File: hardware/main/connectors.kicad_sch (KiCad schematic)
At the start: 3 parts, among them J501 J_UI, J502 J_LED

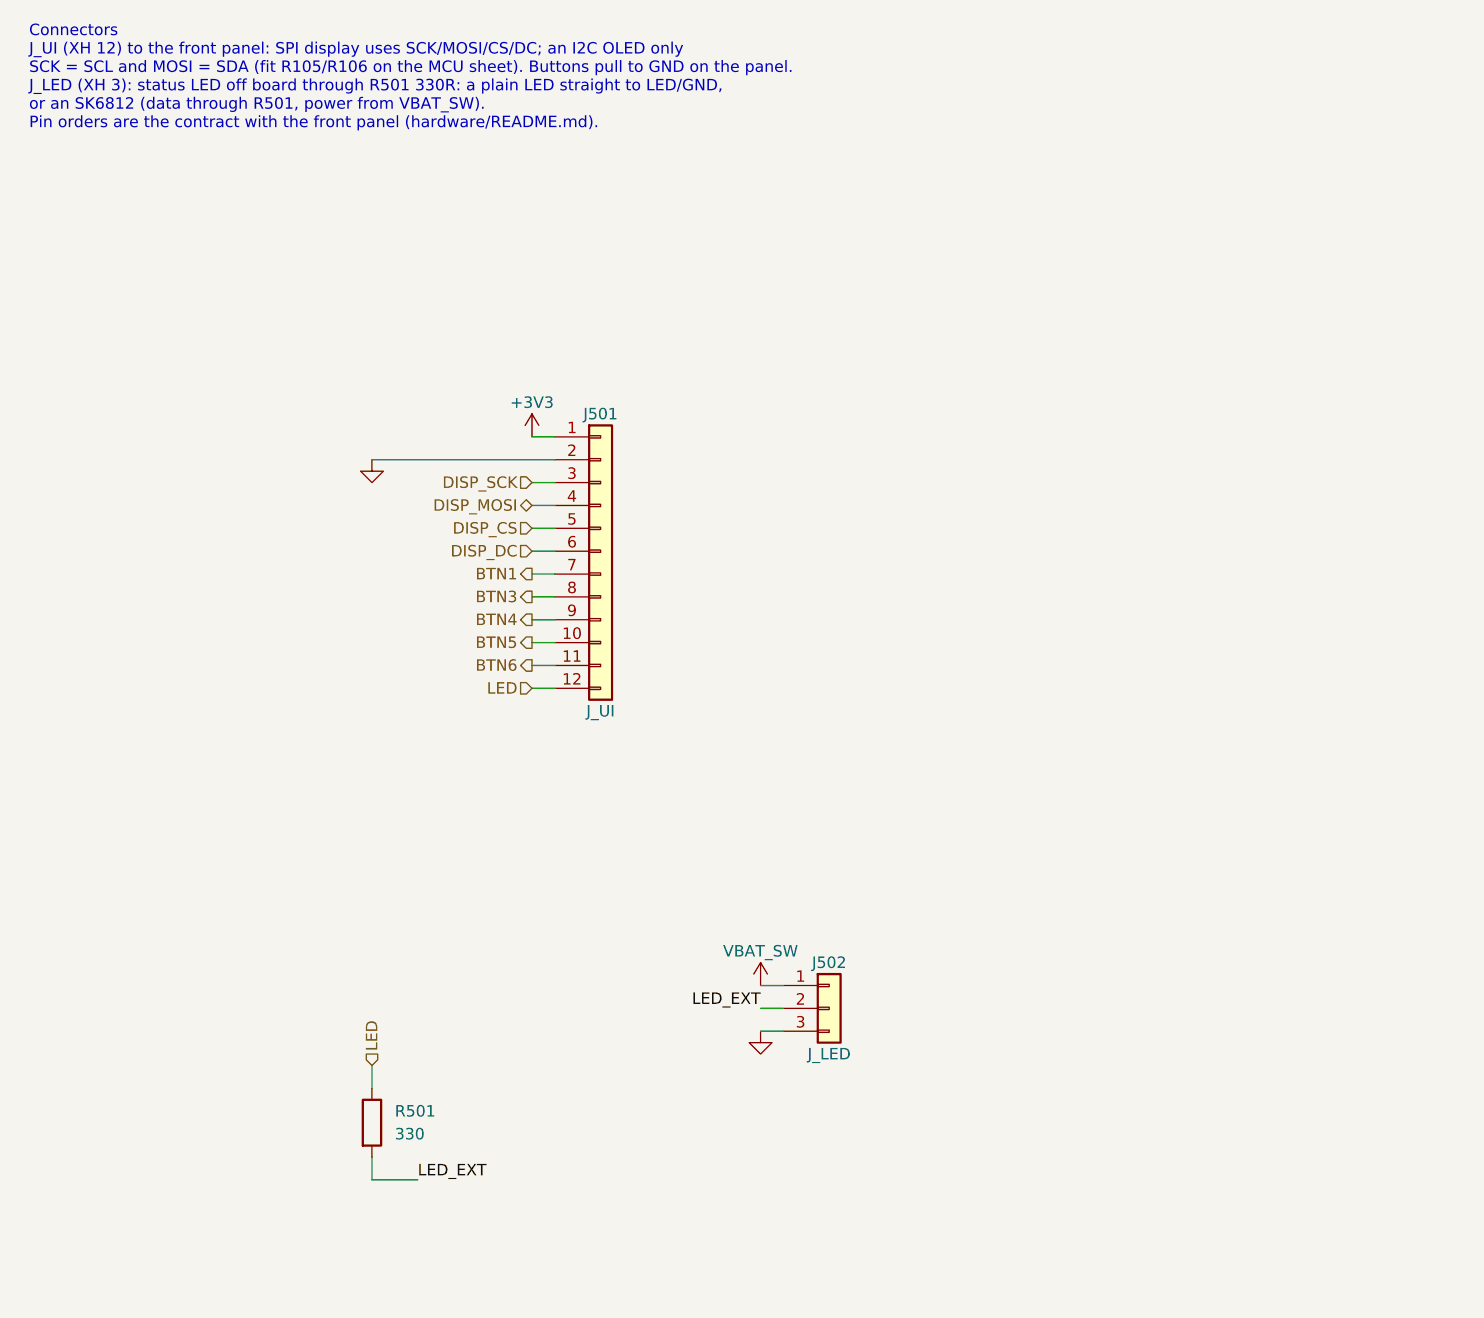
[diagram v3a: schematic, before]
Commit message: hardware: bare USB-C board and front panel (schematics)
J_USB carries CC1/CC2 (XH 6); CC resistors and ESD stay on the main
board. Front panel has only buttons and headers; its LED pin comes
through R501. Boards not yet updated from the schematics.

Co-Authored-By: Claude Opus 5.5 <noreply@anthropic.com>
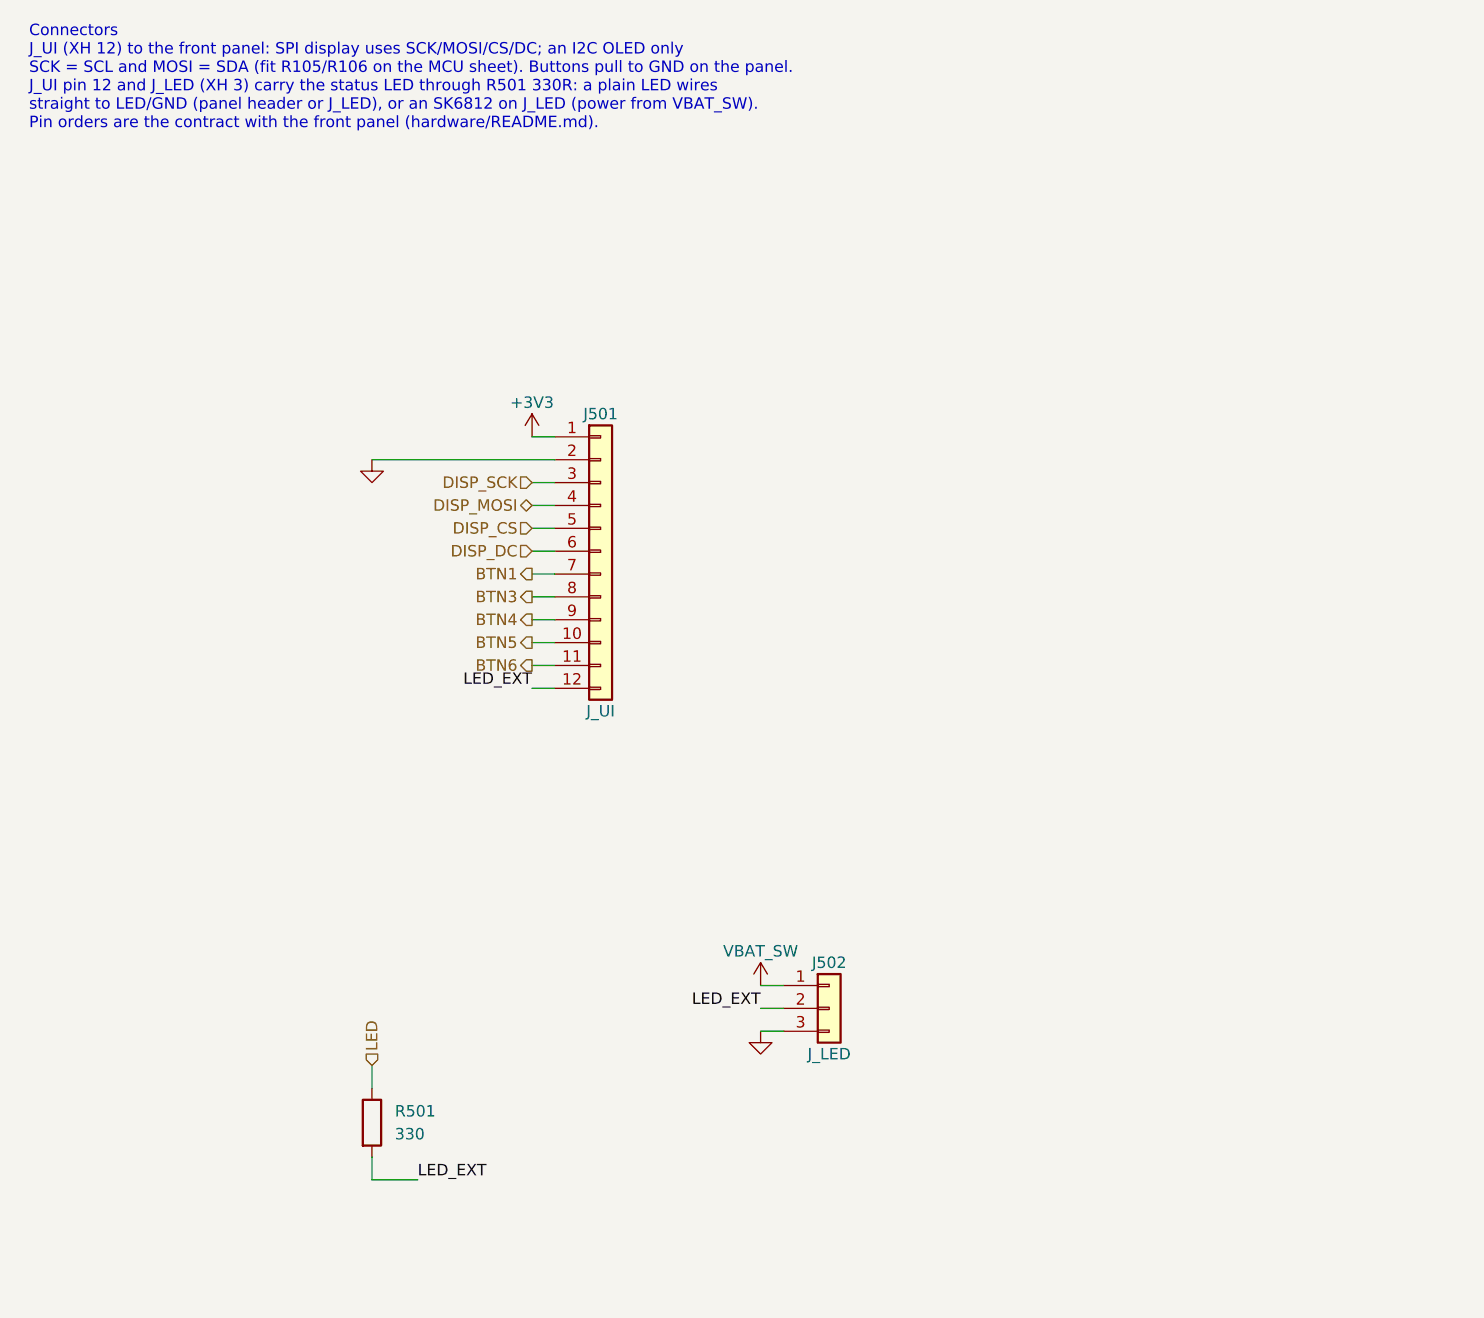
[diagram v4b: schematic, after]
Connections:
- net LED: no longer J501.12 (Pin_12)
- net LED_EXT: now also J501.12 (Pin_12)
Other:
- note added: "Connectors J_UI (XH 12) to the front panel: SPI display uses SCK/MOSI/CS/DC; an I2C OLED only SCK = SCL and MOSI = SDA (fit R105/R106 on the MCU sheet). Buttons pull to GND on the panel. J_UI pin 12 and J_LED (XH 3) carry the status LED through R501 330R: a plain LED wires straight to LED/GND (panel header or J_LED), or an SK6812 on J_LED (power from VBAT_SW). Pin orders are the contract with the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"
- note removed: "Connectors J_UI (XH 12) to the front panel: SPI display uses SCK/MOSI/CS/DC; an I2C OLED only SCK = SCL and MOSI = SDA (fit R105/R106 on the MCU sheet). Buttons pull to GND on the panel. J_LED (XH 3): status LED off board through R501 330R: a plain LED straight to LED/GND, or an SK6812 (data through R501, power from VBAT_SW). Pin orders are the contract with the front panel (hardware/README.md)."

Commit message: hardware: main board routed and labelled, JLC files
- Freerouting (jar, portable Java 25) via scripts/route.py; net classes
  Power 0.8 mm / Supply 0.4 mm so tracks fit the fine-pitch pins.
- Silkscreen pin names and function labels (silk_main.py), references on
  the fab layer, SMD GND pads solid to the pour; board 100 x 58 mm.
- LCSC numbers on all SMD parts (checked on lcsc.com); jlc.py writes the
  Gerber ZIP, BOM and CPL in JLC's formats.

Co-Authored-By: Claude Opus 5.5 <noreply@anthropic.com>
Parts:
- R501: LCSC (none) -> C17630
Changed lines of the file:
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@@
+			)
+		)
+		(property "LCSC" "C17630"
+			(at 0 0 0)
+			(hide yes)
+			(effects
+				(font
+					(size 1.27 1.27)
+				)
 			)
 		)
